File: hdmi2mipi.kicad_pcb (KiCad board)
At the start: 4 copper layers, 55.2 x 55.2 mm, 154 parts, among them J1 USB_C_Receptacle_USB2.0, J2 HDMI_A_1.4, J4 TP, J5 QWIIC, J6 BOOT, J7 SWD, J8 AudioJack3, J9 QWIIC, Q1 BC846, Q2 BC846, Q3 BC846, Q4 BC846, Q5 BC846, Q6 BC846, Q7 2SC2712, U1 SY8079AAC, U10 SY8079AAC, U11 SY8079AAC, U3 SY6280AAC, U4 PCA9306DC, U5 W25Q16JVUXIQ, U6 W25Q16JVUXIQ, U7 RP2040, U8 MS4344, U9 SY8079AAC, X1 SG-210STF, Y1 12MHz

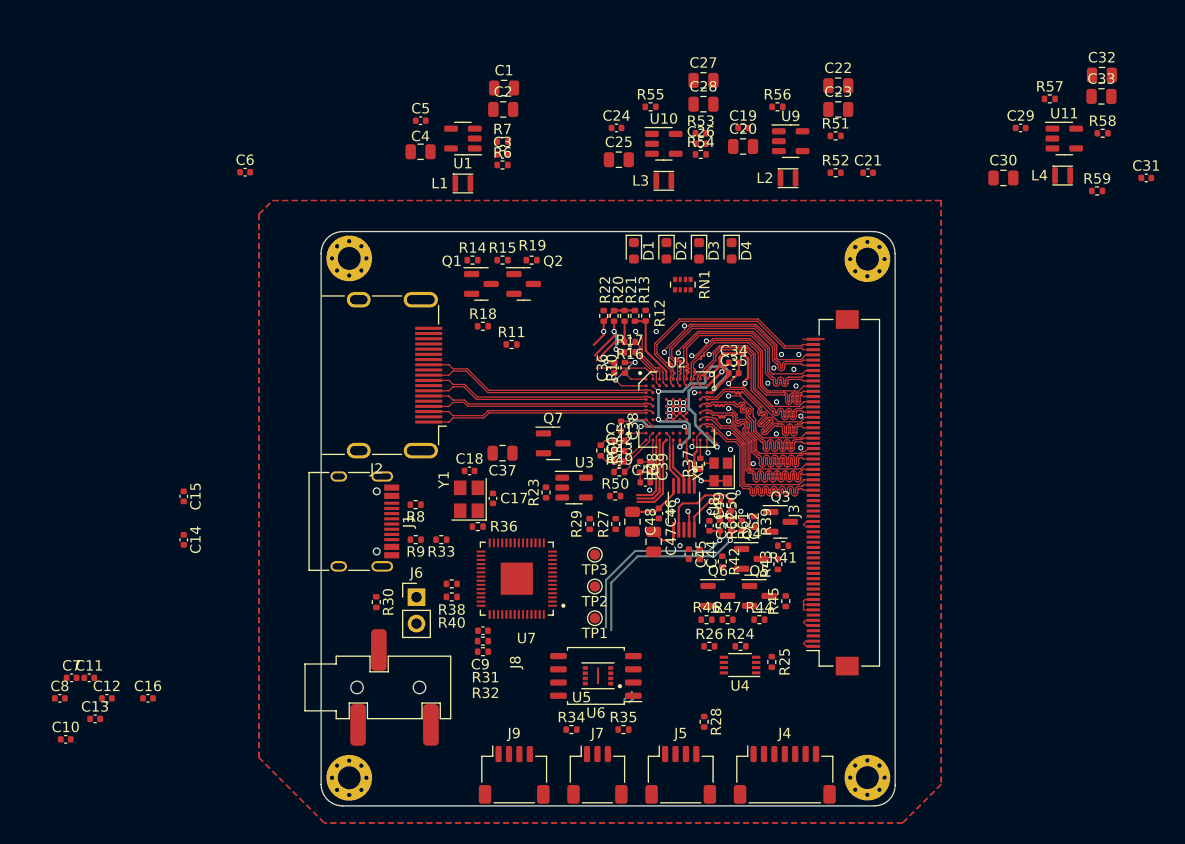
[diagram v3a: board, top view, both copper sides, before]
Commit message: Fix board outline and center circuit board on grid
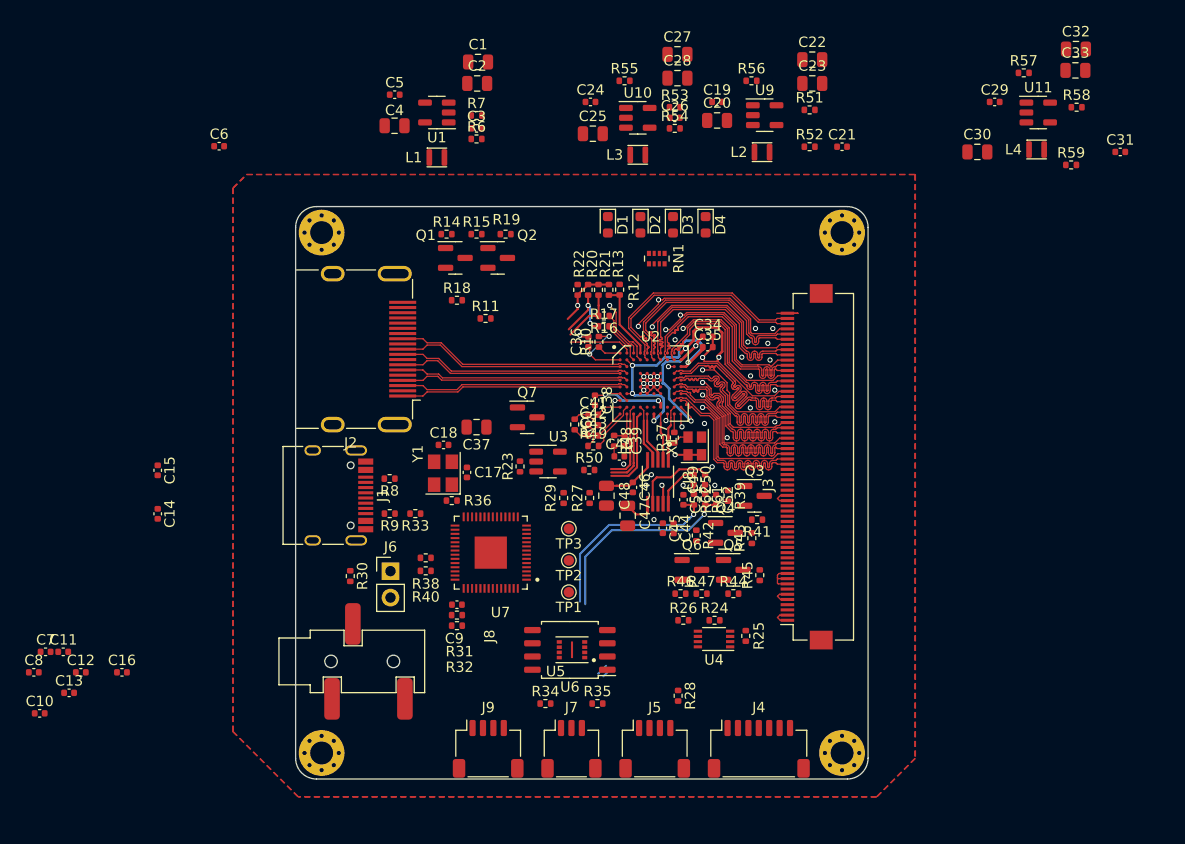
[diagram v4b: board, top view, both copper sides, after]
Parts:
- moved H1 3.63 mm to (-25.0, -25.0)
- moved H4 3.56 mm to (-25.0, 25.0)
- moved L1 3.54 mm to (-13.9, -32.2)
- moved R6 3.54 mm to (-10.1, -34.0)
- moved C1 3.54 mm to (-9.97, -41.4)
- moved C11 3.54 mm to (-49.8, 15.3)
- moved C38 3.54 mm to (1.26, -8.89)
- moved C7 3.54 mm to (-51.5, 15.3)
- moved D2 3.54 mm to (5.63, -25.8)
- moved J6 3.54 mm to (-18.4, 7.53)
- moved Q4 3.54 mm to (13.8, 3.85)
- moved Q6 3.54 mm to (10.6, 7.41)
- moved R44 3.54 mm to (14.6, 9.69)
- moved U8 3.54 mm to (7.31, -1.06)
- moved C10 3.54 mm to (-52.1, 21.2)
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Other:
- board size 55.2 x 55.2 mm -> 55 x 55 mm

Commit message: Backlight driver
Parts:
- added C53: 2.2u, Capacitor_SMD:C_0402_1005Metric, F.Cu at (-45.9, -44.0)
- added C54: ~, Capacitor_SMD:C_0402_1005Metric, F.Cu at (-45.9, -42.0)
- added R1: 10k, Resistor_SMD:R_0402_1005Metric, F.Cu at (-69.1, -33.4)
- added R2: 0, Resistor_SMD:R_0402_1005Metric, F.Cu at (-69.1, -31.4)
- added R3: 10, Resistor_SMD:R_0402_1005Metric, F.Cu at (-69.1, -29.4)
- added R4: 10, Resistor_SMD:R_0402_1005Metric, F.Cu at (-69.1, -27.4)
- added R5: 6.8k, Resistor_SMD:R_0402_1005Metric, F.Cu at (-69.1, -25.4)
- added R63: 50k, Resistor_SMD:R_0402_1005Metric, F.Cu at (-69.1, -23.4)
- added R64: 100k, Resistor_SMD:R_0402_1005Metric, F.Cu at (-69.1, -21.4)
- added TP4: TestPoint, TestPoint:TestPoint_Pad_D2.0mm, F.Cu at (-49.4, -43.0)
- added TP5: TestPoint, TestPoint:TestPoint_Pad_D2.0mm, F.Cu at (-49.4, -38.9)
- added U12: ~, Package_TO_SOT_SMD:SOT-23-6, F.Cu at (-63.5, -31.2)
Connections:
- J3 pad 13: unconnected-(J3-5.8v-VEE-Pad13) -> Net-(J3-5.8v-VEE)
- J3 pad 14: unconnected-(J3-5.8v-VDD-Pad14) -> Net-(J3-5.8v-VDD)
- J3 pad 27: Net-(J3-3.3-S2) -> Net-(J3-3.3-S1)
- Q3 pad 3: Net-(J3-3.3-S2) -> Net-(J3-3.3-S1)
- R41 pad 2: Net-(J3-3.3-S2) -> Net-(J3-3.3-S1)
- U7 pad 29: unconnected-(U7-GPIO18-Pad29) -> BL_EN
- U7 pad 30: unconnected-(U7-GPIO19-Pad30) -> BL_PWM
